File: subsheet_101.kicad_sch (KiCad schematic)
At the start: 6 parts, among them U101 ST_BLITTER_PHY

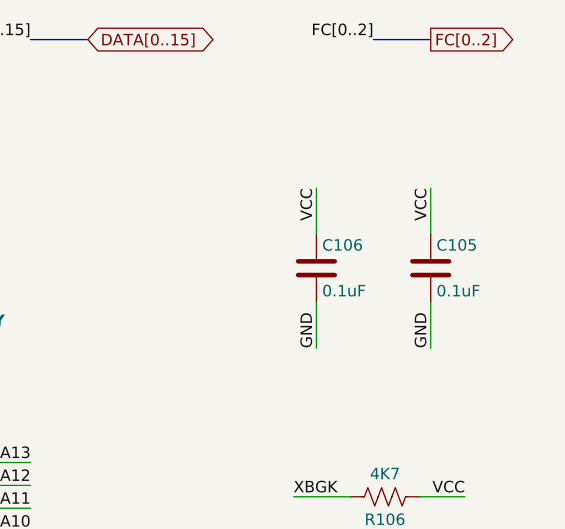
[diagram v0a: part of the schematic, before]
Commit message: Resolves #3 : [schematic] annotate video port with signal name
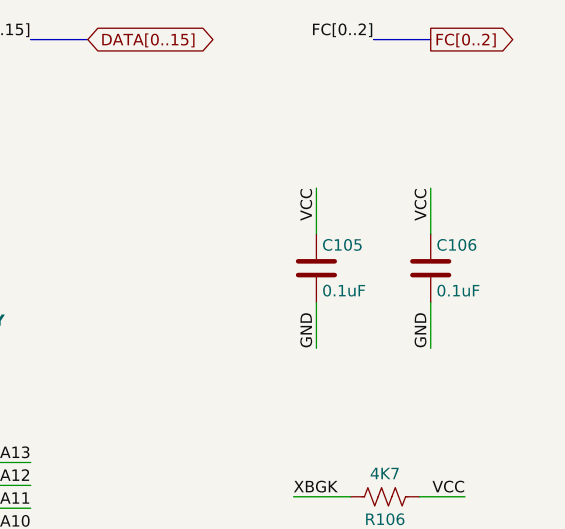
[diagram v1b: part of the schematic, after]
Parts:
- renumbered C106 to C105, C105 to C106
